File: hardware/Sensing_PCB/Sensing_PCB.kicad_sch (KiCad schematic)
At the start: 8 parts, among them J1 B5B-XH-A, U1 FSG005WNPB, U3 LMC6484IN_NOPB, U4 Pico

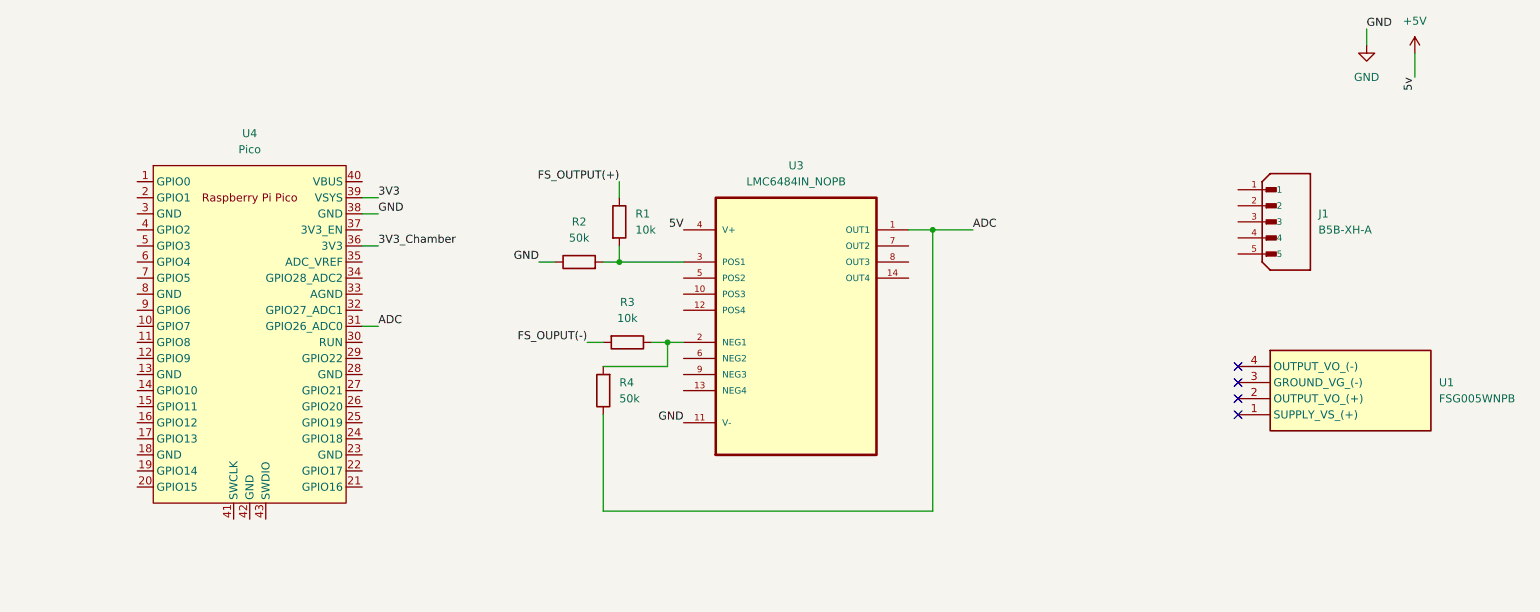
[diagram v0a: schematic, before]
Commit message: Add Rev.1 of Sender PCB
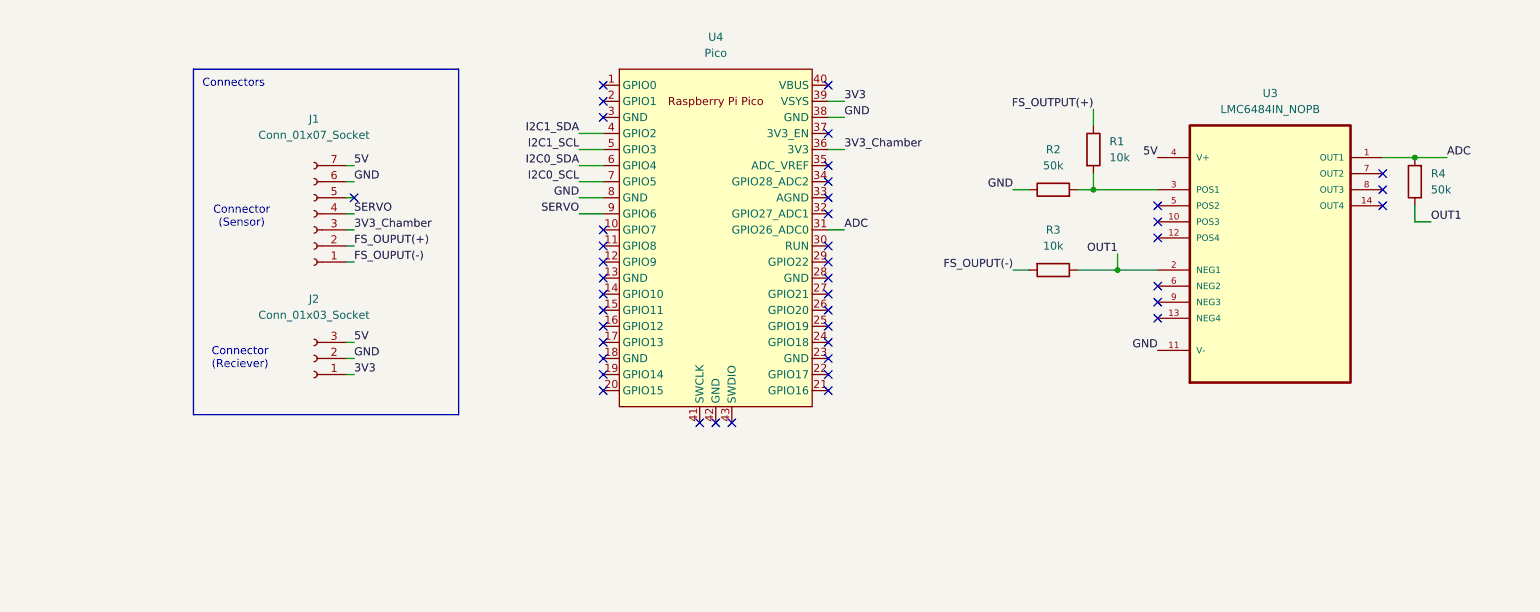
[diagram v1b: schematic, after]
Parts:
- removed J1: B5B-XH-A, B5B-XH-A:JST_B5B-XH-A, symbol B5B-XH-A:B5B-XH-A
- removed U1: FSG005WNPB, FSG005WNPB, symbol FSG005WNPB:FSG005WNPB
- added J1: Conn_01x07_Socket, Connector_JST:JST_PH_B7B-PH-K_1x07_P2.00mm_Vertical, symbol Connector:Conn_01x07_Socket
- added J2: Conn_01x03_Socket, Connector_JST:JST_PH_B3B-PH-K_1x03_P2.00mm_Vertical, symbol Connector:Conn_01x03_Socket
- R1, R2, R3, R4: footprint (none) -> Resistor_SMD:R_0603_1608Metric
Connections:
- net 3V3: now also J2.1 (Pin_1)
- net 3V3_Chamber: now also J1.3 (Pin_3)
- net 5V: now also J1.7 (Pin_7), J2.3 (Pin_3)
- net ADC: now also R4.2; no longer R4.1
- net FS_OUPUT(-): now also J1.1 (Pin_1)
- net GND: now also U4.8 (GND), J1.6 (Pin_6), J2.2 (Pin_2)
- net I2C1_SDA: now reaches U4.4 (GPIO2)
- net I2C1_SCL: now reaches U4.5 (GPIO3)
- net I2C0_SDA: now reaches U4.6 (GPIO4)
- net I2C0_SCL: now reaches U4.7 (GPIO5)
- net SERVO: now reaches U4.9 (GPIO6)
- net SERVO: now also J1.4 (Pin_4)
- net OUT1: now reaches R3.1, U3.2 (NEG1)
- net OUT1: now also R4.1; no longer R4.2
- new net FS_OUPUT(+): J1.2 (Pin_2)
- no-connect marks 4 -> 43
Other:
- note added: "Connector (Reciever)"
- note added: "Connector (Sensor)"
- note added: "Connectors"
- title: OPEL Sensing Reciever -> OPEL Sensing Sender
- moved on the sheet: R1, R2, R3, R4, U3, U4

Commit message: Update Sender PCB
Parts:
- removed J2: Conn_01x03_Socket, Connector_JST:JST_PH_B3B-PH-K_1x03_P2.00mm_Vertical, symbol Connector:Conn_01x03_Socket
- added H1, H2, H3, H4: MountingHole, MountingHole:MountingHole_2.2mm_M2, symbol Mechanical:MountingHole
- added J2: Conn_01x04_Socket, Connector_JST:JST_PH_B4B-PH-K_1x04_P2.00mm_Vertical, symbol Connector:Conn_01x04_Socket
- added J3: Conn_01x03_Socket, Connector_JST:JST_PH_B3B-PH-K_1x03_P2.00mm_Vertical, symbol Connector:Conn_01x03_Socket
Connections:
- net FS_OUPUT(+) is gone; now on net I2C1_SDA: J1.2 (Pin_2)
- net 3V3: now also J1.6 (Pin_6)
- net 3V3_Chamber: now also U3.4 (V+), J2.1 (Pin_1); no longer J1.3 (Pin_3)
- net 5V: now also J3.2 (Pin_2); no longer U3.4 (V+)
- net FS_OUTPUT(+): now also J2.2 (Pin_2)
- net GND: now also J1.1 (Pin_1), U4.23 (GND), U4.28 (GND), J2.3 (Pin_3), J3.1 (Pin_1); no longer J1.6 (Pin_6)
- net I2C0_SCL: now also J1.5 (Pin_5)
- net I2C0_SDA: now also J1.4 (Pin_4)
- net I2C1_SCL: now also J1.3 (Pin_3)
- net SERVO: now also J3.3 (Pin_3); no longer J1.4 (Pin_4)
- net FS_OUPUT(-) renamed FS_OUTPUT(-)
- net FS_OUTPUT(-): now also J2.4 (Pin_4); no longer J1.1 (Pin_1)
- no-connect marks 43 -> 40
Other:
- note added: "Connector (Servo)"
